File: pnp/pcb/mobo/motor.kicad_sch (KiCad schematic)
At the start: 8 parts, among them M4 Stepper_Motor

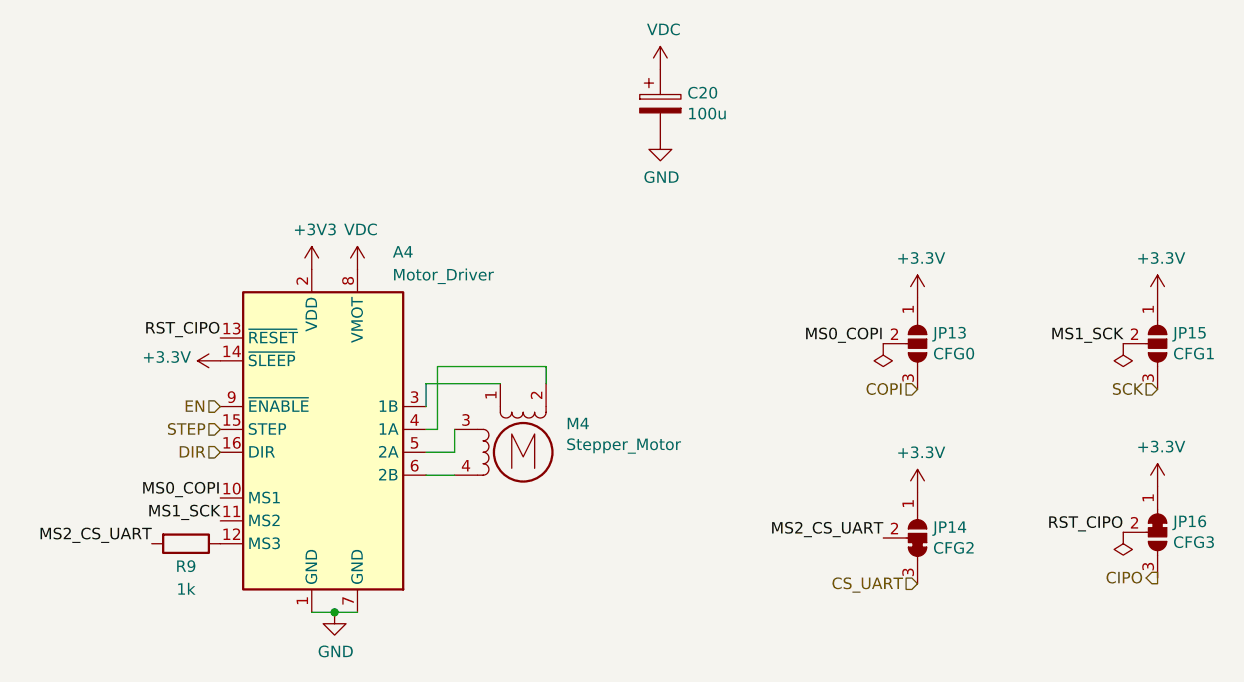
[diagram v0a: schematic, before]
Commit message: Clean the ERC
- Changed some broken symbol links
- Changed all _Limit netlabels to _LIMIT

ERC list is now empty.
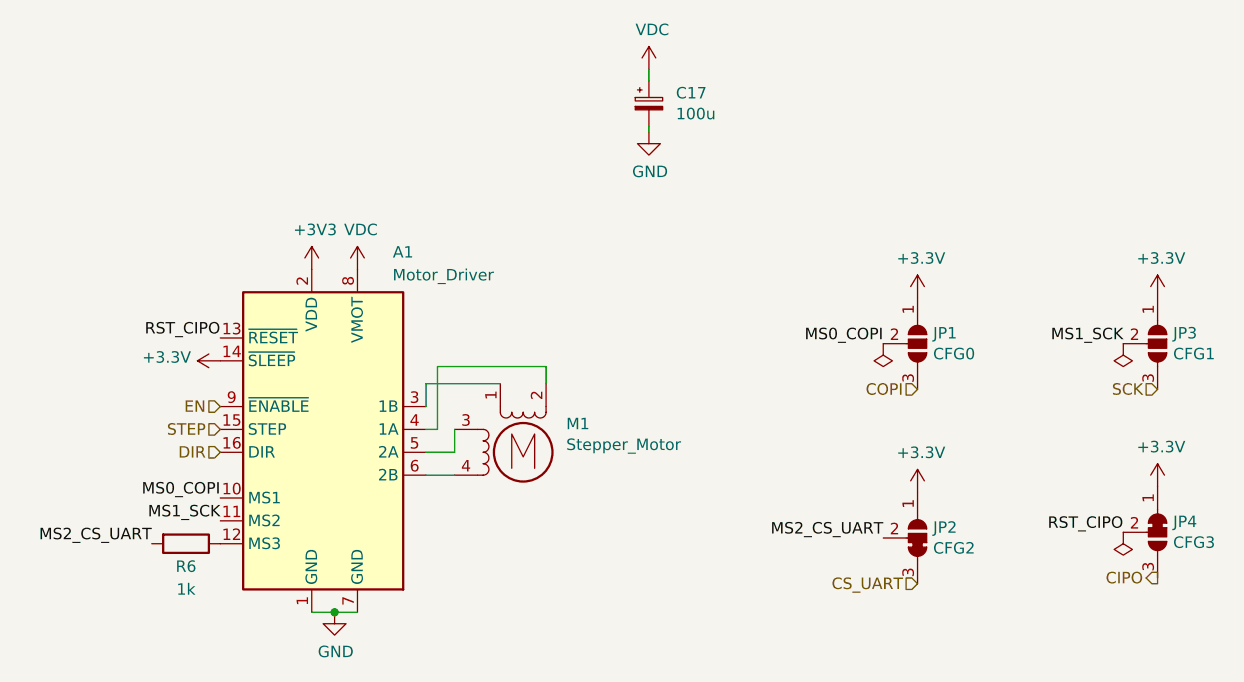
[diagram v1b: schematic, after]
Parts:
- C17: renamed from C20; symbol Device:CP -> Device:C_Polarized_Small
- renumbered A4 to A1, JP13 to JP1, JP14 to JP2, JP15 to JP3, JP16 to JP4, M4 to M1, R9 to R6
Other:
- moved on the sheet: C17
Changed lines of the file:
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@@
+    (stroke (width 0) (type default) (color 0 0 0 0))
+  )
+  (wire (pts (xy 152.4 55.245) (xy 152.4 56.515))
     (stroke (width 0) (type default) (color 0 0 0 0))
   )
@@
     (stroke (width 0) (type default) (color 0 0 0 0))
   )
+  (wire (pts (xy 152.4 61.595) (xy 152.4 62.23))
+    (stroke (width 0) (type default) (color 0 0 0 0))
+  )
   (label "RST_CIPO" (at 104.775 85.09 180)
     (effects (font (size 1.27 1.27)) (justify right bottom))
@@
   (symbol (lib_id "Device:R") (at 100.965 107.95 270)
     (in_bom yes) (on_board yes)
-    (property "Reference" "R9" (id 0) (at 100.965 110.49 90))
+    (property "Reference" "R6" (id 0) (at 100.965 110.49 90))
     (property "Value" "1k" (id 1) (at 100.965 113.03 90))
     (property "Footprint" "Resistor_SMD:R_0805_2012Metric" (id 2) (at 100.965 106.172 90)
@@
   (symbol (lib_id "Driver_Motor:Pololu_Breakout_A4988") (at 114.935 95.25 0)
     (in_bom yes) (on_board yes)
-    (property "Reference" "A4" (id 0) (at 125.095 75.565 0))
+    (property "Reference" "A1" (id 0) (at 125.095 75.565 0))
     (property "Value" "Motor_Driver" (id 1) (at 129.54 78.105 0))
     (property "Footprint" "Module:Pololu_Breakout-16_15.2x20.3mm" (id 2) (at 121.92 114.3 0)
@@
   (symbol (lib_id "Motor:Stepper_Motor_bipolar") (at 138.43 97.79 0)
     (in_bom yes) (on_board yes)
-    (property "Reference" "M4" (id 0) (at 143.2052 94.6404 0)
+    (property "Reference" "M1" (id 0) (at 143.2052 94.6404 0)
       (effects (font (size 1.27 1.27)) (justify left))
     )
@@
     (pin "1")
   )
-  (symbol (lib_id "Device:CP") (at 153.67 59.055 0)
-    (in_bom yes) (on_board yes)
-    (property "Reference" "C20" (id 0) (at 156.6672 57.8866 0)
-      (effects (font (size 1.27 1.27)) (justify left))
-    )
-    (property "Value" "100u" (id 1) (at 156.6672 60.198 0)
-      (effects (font (size 1.27 1.27)) (justify left))
-    )
-    (property "Footprint" "Capacitor_SMD:CP_Elec_6.3x7.7" (id 2) (at 154.6352 62.865 0)
-      (effects (font (size 1.27 1.27)) hide)
-    )
-    (property "Datasheet" "" (id 3) (at 153.67 59.055 0)
-      (effects (font (size 1.27 1.27)) hide)
-    )
-    (property "Digikey" "493-2203-1-ND" (id 4) (at 153.67 59.055 0)
-      (effects (font (size 1.27 1.27)) hide)
-    )
-    (property "JLCPCB" "C99837" (id 5) (at 153.67 59.055 0)
-      (effects (font (size 1.27 1.27)) hide)
-    )
-    (property "LCSC" "C3339" (id 6) (at 153.67 59.055 0)
-      (effects (font (size 1.27 1.27)) hide)
-    )
-    (property "Mouser" "647-UWT1V101MCL1S" (id 7) (at 153.67 59.055 0)
-      (effects (font (size 1.27 1.27)) hide)
-    )
-    (pin "1")
-    (pin "2")
-  )
-  (symbol (lib_id "power:VDC") (at 153.67 55.245 0)
-    (in_bom yes) (on_board yes)
-    (property "Reference" "#PWR057" (id 0) (at 153.67 57.785 0)
-      (effects (font (size 1.27 1.27)) hide)
-    )
-    (property "Value" "VDC" (id 1) (at 154.051 50.8508 0))
-    (property "Footprint" "" (id 2) (at 153.67 55.245 0)
-      (effects (font (size 1.27 1.27)) hide)
-    )
-    (property "Datasheet" "" (id 3) (at 153.67 55.245 0)
-      (effects (font (size 1.27 1.27)) hide)
-    )
-    (pin "1")
-  )
-  (symbol (lib_id "power:GND") (at 153.67 62.865 0)
-    (in_bom yes) (on_board yes)
-    (property "Reference" "#PWR058" (id 0) (at 153.67 69.215 0)
-      (effects (font (size 1.27 1.27)) hide)
-    )
-    (property "Value" "GND" (id 1) (at 153.797 67.2592 0))
-    (property "Footprint" "" (id 2) (at 153.67 62.865 0)
-      (effects (font (size 1.27 1.27)) hide)
-    )
-    (property "Datasheet" "" (id 3) (at 153.67 62.865 0)
+  (symbol (lib_id "Device:C_Polarized_Small") (at 152.4 59.055 0)
+    (in_bom yes) (on_board yes)
+    (property "Reference" "C17" (id 0) (at 155.3972 57.8866 0)
+      (effects (font (size 1.27 1.27)) (justify left))
+    )
+    (property "Value" "100u" (id 1) (at 155.3972 60.198 0)
+      (effects (font (size 1.27 1.27)) (justify left))
+    )
+    (property "Footprint" "Capacitor_SMD:CP_Elec_6.3x7.7" (id 2) (at 153.3652 62.865 0)
+      (effects (font (size 1.27 1.27)) hide)
+    )
+    (property "Datasheet" "" (id 3) (at 152.4 59.055 0)
+      (effects (font (size 1.27 1.27)) hide)
+    )
+    (property "Digikey" "493-2203-1-ND" (id 4) (at 152.4 59.055 0)
+      (effects (font (size 1.27 1.27)) hide)
+    )
+    (property "JLCPCB" "C99837" (id 5) (at 152.4 59.055 0)
+      (effects (font (size 1.27 1.27)) hide)
+    )
+    (property "LCSC" "C3339" (id 6) (at 152.4 59.055 0)
+      (effects (font (size 1.27 1.27)) hide)
+    )
+    (property "Mouser" "647-UWT1V101MCL1S" (id 7) (at 152.4 59.055 0)
+      (effects (font (size 1.27 1.27)) hide)
+    )
+    (pin "1")
+    (pin "2")
+  )
+  (symbol (lib_id "power:VDC") (at 152.4 55.245 0)
+    (in_bom yes) (on_board yes)
+    (property "Reference" "#PWR057" (id 0) (at 152.4 57.785 0)
+      (effects (font (size 1.27 1.27)) hide)
+    )
+    (property "Value" "VDC" (id 1) (at 152.781 50.8508 0))
+    (property "Footprint" "" (id 2) (at 152.4 55.245 0)
+      (effects (font (size 1.27 1.27)) hide)
+    )
+    (property "Datasheet" "" (id 3) (at 152.4 55.245 0)
+      (effects (font (size 1.27 1.27)) hide)
+    )
+    (pin "1")
+  )
+  (symbol (lib_id "power:GND") (at 152.4 62.23 0)
+    (in_bom yes) (on_board yes)
+    (property "Reference" "#PWR058" (id 0) (at 152.4 68.58 0)
+      (effects (font (size 1.27 1.27)) hide)
+    )
+    (property "Value" "GND" (id 1) (at 152.527 66.6242 0))
+    (property "Footprint" "" (id 2) (at 152.4 62.23 0)
+      (effects (font (size 1.27 1.27)) hide)
+    )
+    (property "Datasheet" "" (id 3) (at 152.4 62.23 0)
       (effects (font (size 1.27 1.27)) hide)
     )
@@
   (symbol (lib_id "Jumper:SolderJumper_3_Open") (at 182.245 85.725 270)
     (in_bom yes) (on_board yes)
-    (property "Reference" "JP13" (id 0) (at 183.9722 84.5566 90)
+    (property "Reference" "JP1" (id 0) (at 183.9722 84.5566 90)
       (effects (font (size 1.27 1.27)) (justify left))
     )
@@
   (symbol (lib_id "Jumper:SolderJumper_3_Bridged12") (at 208.915 106.68 270)
     (in_bom yes) (on_board yes)
-    (property "Reference" "JP16" (id 0) (at 210.6422 105.5116 90)
+    (property "Reference" "JP4" (id 0) (at 210.6422 105.5116 90)
       (effects (font (size 1.27 1.27)) (justify left))
     )
@@
   (symbol (lib_id "Jumper:SolderJumper_3_Open") (at 208.915 85.725 270)
     (in_bom yes) (on_board yes)
-    (property "Reference" "JP15" (id 0) (at 210.6422 84.5566 90)
+    (property "Reference" "JP3" (id 0) (at 210.6422 84.5566 90)
       (effects (font (size 1.27 1.27)) (justify left))
     )
@@
   (symbol (lib_id "index:SolderJumper_3_Bridged23") (at 182.245 107.315 270) (mirror x)
     (in_bom yes) (on_board yes)
-    (property "Reference" "JP14" (id 0) (at 183.9722 106.1466 90)
-      (effects (font (size 1.27 1.27)) (justify left))
-    )
+    (property "Reference" "JP2" (id 0) (at 183.9722 106.1466 90)
+      (effects (font (size 1.27 1.27)) (justify left))
+    )
